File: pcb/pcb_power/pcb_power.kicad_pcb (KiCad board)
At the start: 2 copper layers, 100 x 100 mm, 17 parts, among them J10 Conn_01x04, J11 Conn_01x04, J40 XT30, K10 FINDER-40.41, K11 FINDER-40.41, Q40 BD139, Q41 BD139, Q42 BD249C, Q43 BD249C

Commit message: fin board
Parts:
- added D20: BYG22B, Diode_SMD:D_SMA, B.Cu at (2.50, 18.0)
- added D21: BYG22B, Diode_SMD:D_SMA, B.Cu at (-3.00, 36.5)
- C30, C31: footprint Capacitor_THT:CP_Radial_D14.0mm_P7.50mm -> Capacitor_THT:CP_Radial_D22.0mm_P10.00mm_SnapIn
- J10: value Conn_01x04 -> JST_B4B-XH-A
- J11: value Conn_01x04 -> JST_B4P-VH; footprint Connector_JST:JST_VH_B4P-VH-FB-B_1x04_P3.96mm_Vertical -> Connector_JST:JST_VH_B4P-VH_1x04_P3.96mm_Vertical
- moved J12 32.1 mm to (70.5, 62.0), turned to 180 degrees
- moved R40 12.8 mm to (39.1, 70.0), turned to 0 degrees
- moved J11 12.6 mm to (-12.6, 62.4), turned to 0 degrees
- moved J10 11.5 mm to (11.3, 63.8)
- moved C31 7.84 mm to (64.8, 19.8), turned to 0 degrees
- moved C30 6.58 mm to (65.0, 43.0), turned to 0 degrees
- moved R41 0.20 mm to (39.1, 62.0)
- renumbered J40 to J12, K11 to K20, K10 to K21, Q42 to Q40, Q40 to Q41, Q43 to Q42, Q41 to Q43
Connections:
- J10 pad 1: /Tab selector/Relay_GND -> /Tab selector/Relay1
- J10 pad 2: /Tab selector/Relay1 -> /Tab selector/Relay2
- J10 pad 3: /Tab selector/Relay2 -> /Tab selector/Relay_VCC
- J11 pad 1: /Rectifier/AC1 -> /Tab selector/30V_AC
- J11 pad 2: /Tab selector/10V_AC -> /Tab selector/20V_AC
- J11 pad 3: /Tab selector/20V_AC -> /Tab selector/10V_AC
- J11 pad 4: /Tab selector/30V_AC -> /Rectifier/AC1
- K20 pad A2: /Tab selector/Relay_GND -> /Tab selector/Relay_VCC
- K21 pad A2: /Tab selector/Relay_GND -> /Tab selector/Relay_VCC
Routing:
- net /Power_transistors/collector: track 108.0 -> 20.5 mm
- net /Tab selector/Relay2: track 0.00 -> 71.7 mm
- net /Tab selector/Relay_VCC: track 0.00 -> 65.1 mm
- net /Rectifier/AC2: track 58.1 -> 0.00 mm
- net /Tab selector/Relay1: track 0.00 -> 47.9 mm
- net /Power_transistors/base: track 0.00 -> 43.9 mm
- net /Rectifier/-DC: track 26.7 -> 0.00 mm
- net /Power_transistors/pwr_e1: track 0.00 -> 23.8 mm
- net /Rectifier/AC1: track 77.9 -> 55.3 mm
- net /Power_transistors/pwr_e2: track 0.00 -> 17.2 mm
- net /Tab selector/10V_AC: track 20.2 -> 22.2 mm
- net /Power_transistors/pwr_eb1: track 13.3 -> 12.2 mm
- net /Tab selector/20V_AC: track 17.7 -> 16.8 mm
- added copper zone on F.Cu, net /Power_transistors/collector
- added copper zone on B.Cu, net /Power_transistors/emitter
- added copper zone on B.Cu, net /Rectifier/-DC
- added copper zone on B.Cu, net /Rectifier/AC1
- added copper zone on B.Cu, net /Rectifier/AC2
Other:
- board size 100 x 100 mm -> 100 x 79 mm
- board text added: "0VAC"
- board text added: "10VAC"
- board text added: "12V"
- board text added: "20VAC"
- board text added: "26.02.2024"
- board text added: "30VAC"
- board text added: "Author:"
- board text added: "Base"
- board text added: "Date:"
- board text added: "Dominik Workshop"
- board text added: "Linear power supply 2"
- board text added: "Relay 1"
- board text added: "power board V1.0"

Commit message: centered pcb
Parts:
- moved C31 132.4 mm to (181.8, 81.8)
- moved J10 132.4 mm to (128.3, 125.8)
- moved Q42 132.4 mm to (158.2, 117.0)
- moved R40 132.4 mm to (156.1, 132.0)
- moved R41 132.4 mm to (156.1, 124.0)
- moved C30 132.4 mm to (182.0, 105.0)
- moved D20 132.4 mm to (119.5, 80.0)
- moved D21 132.4 mm to (114.0, 98.5)
- moved D30 132.4 mm to (143.0, 87.0)
- moved D31 132.4 mm to (154.0, 87.0)
- moved D32 132.4 mm to (132.0, 87.0)
- moved D33 132.4 mm to (165.0, 87.0)
- moved J11 132.4 mm to (104.4, 124.3)
- moved J12 132.4 mm to (187.5, 124.0)
- moved K20 132.4 mm to (124.0, 80.0)
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
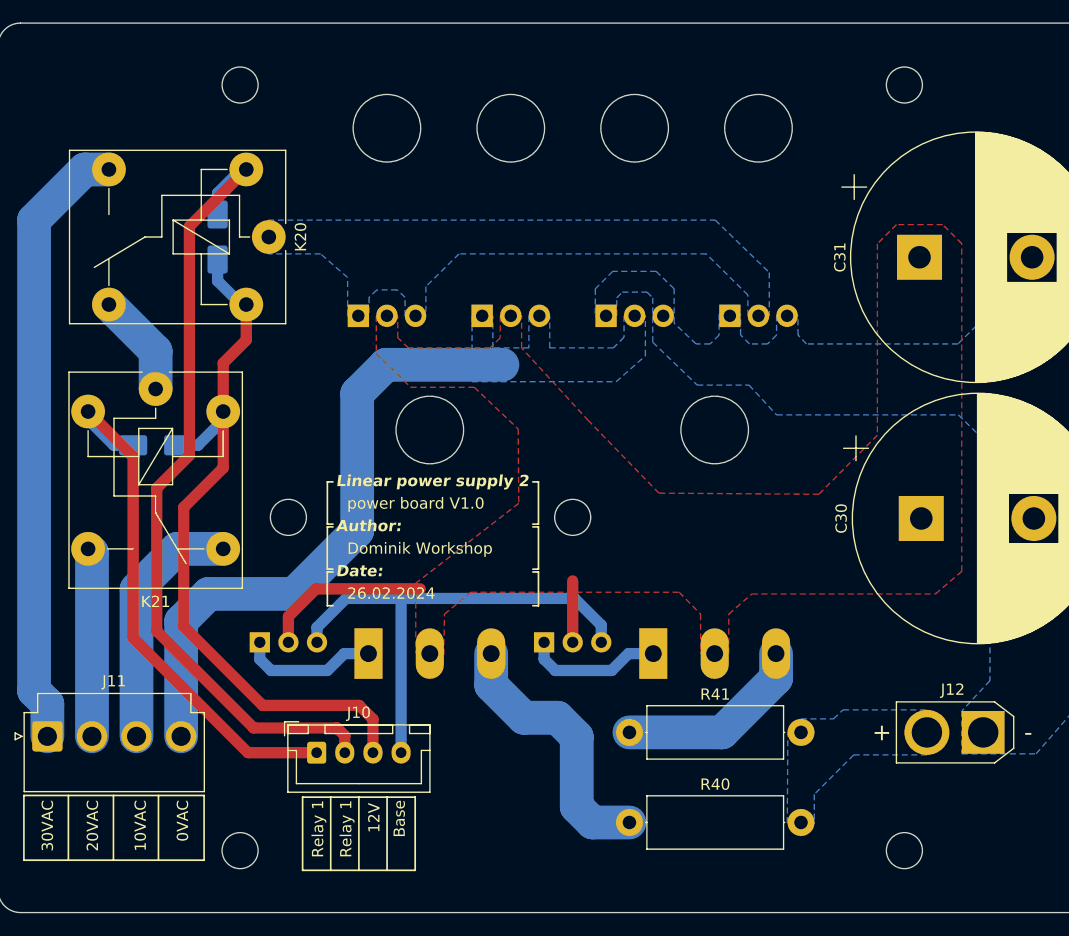
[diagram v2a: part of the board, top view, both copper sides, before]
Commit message: drc set, added icons, teardrops, info
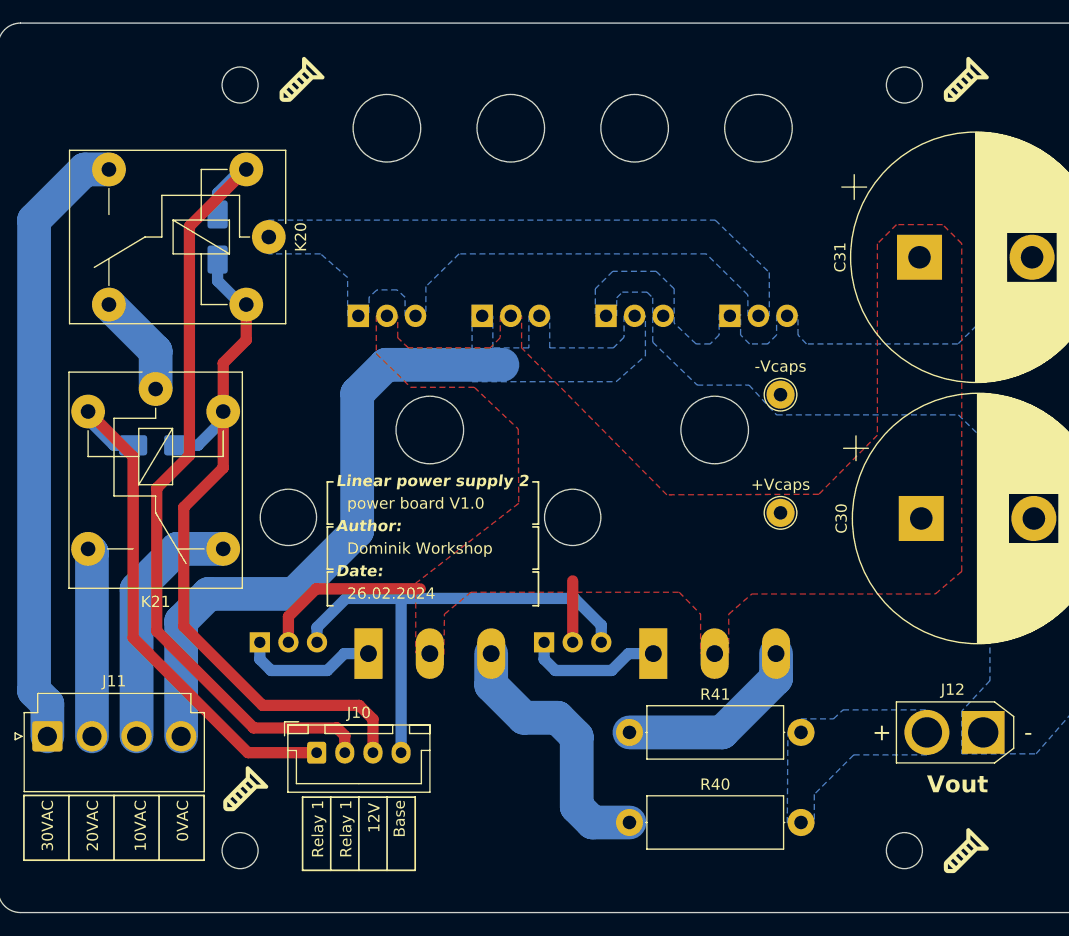
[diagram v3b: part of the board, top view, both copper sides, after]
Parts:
- added +Vcaps: TestPoint_THTPad_D2.5mm_Drill1.2mm, TestPoint:TestPoint_THTPad_D2.5mm_Drill1.2mm, F.Cu at (169.5, 104.5)
- added -Vcaps: TestPoint_THTPad_D2.5mm_Drill1.2mm, TestPoint:TestPoint_THTPad_D2.5mm_Drill1.2mm, F.Cu at (169.5, 94.0)
- added G***: LOGO, logos.preety:screw, F.Cu at (122.0, 129.0)
- added G***: LOGO, logos.preety:screw, F.Cu at (127.0, 66.0)
- added G***: LOGO, logos.preety:screw, F.Cu at (186.0, 66.0)
- added G***: LOGO, logos.preety:screw, F.Cu at (186.0, 134.5)
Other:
- rule pad_to_mask_clearance: 0 -> 0.038
- board text added: "Vout"

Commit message: minor changes, final?
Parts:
- moved J10 60.5 mm to (84.3, 84.3)
- moved R40 60.5 mm to (112.1, 90.5)
- moved R41 60.5 mm to (112.1, 82.5)
- moved +Vcaps 60.5 mm to (125.5, 63.0)
- moved C30 60.5 mm to (138.0, 63.5)
- moved C31 60.5 mm to (137.8, 40.3)
- moved D20 60.5 mm to (75.5, 38.5)
- moved D21 60.5 mm to (70.0, 57.0)
- moved D30 60.5 mm to (99.0, 45.5)
- moved D31 60.5 mm to (110.0, 45.5)
- moved D32 60.5 mm to (88.0, 45.5)
- moved D33 60.5 mm to (121.0, 45.5)
- moved G*** 60.5 mm to (78.0, 87.5)
- moved G*** 60.5 mm to (83.0, 24.5)
- moved G*** 60.5 mm to (142.0, 24.5)
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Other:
- board text added: "Relay_1"
- board text added: "V0_AC"
- board text added: "V1_AC"
- board text added: "V2_AC"
- board text added: "V3_AC"
- board text removed: "0VAC"
- board text removed: "10VAC"
- board text removed: "20VAC"
- board text removed: "30VAC"
- board text removed: "Relay 1"
